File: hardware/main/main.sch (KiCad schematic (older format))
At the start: 2 parts, among them J101 Conn_01x06_Male, J102 Conn_01x06_Male

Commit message: Alimentação de 12V criada no Charger, que recebe 18V do Controller
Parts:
- removed J102: Conn_01x06_Male, symbol Connector:Conn_01x06_Male
- added J102: Conn_01x07_Male, symbol Connector:Conn_01x07_Male
- J101: value Conn_01x06_Male -> Conn_01x07_Male; symbol Connector:Conn_01x06_Male -> Connector:Conn_01x07_Male
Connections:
- net CONTROLLER/Charge: now also J102.6 (Pin_6)
- net CONTROLLER/GND: now also J102.1 (Pin_1), J102.3 (Pin_3), J102.5 (Pin_5)
- net CONTROLLER/RL_OFF: now also J102.2 (Pin_2)
- net CONTROLLER/RL_ON: now also J102.4 (Pin_4)
- new net CHARGER/+18V_IN: J101.7 (Pin_7)
- new net CONTROLLER/+18V_OUT: J102.7 (Pin_7)
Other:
- note added: "TO-DO LIST:\n [x] Separar a abstração das duas placas\n\n [x] Criar conexão entre as duas placas\n\n [x] Nomear componentes;\n\n [x] Passar alimentação para o Charger;\n\n [x] Criar fonte 12V no Charger\n\n [_] Adicionar snubbers para os relés (olhar na simulação);\n\n [_] Passar o condicionamento do sinal para o Charger;\n"
- note removed: "TO-DO LIST:\n [x] Separar a abstração das duas placas\n\n [x] Criar conexão entre as duas placas\n\n [x] Nomear componentes;\n\n [_] Passar alimentação para o Charger;\n\n [_] Adicionar snubbers para os relés (olhar na simulação);\n\n [_] Passar o condicionamento do sinal para o Charger;\n"
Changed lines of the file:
@@
 $EndDescr
 $Sheet
-S 3050 2400 1200 950
+S 3050 2400 1200 1050
 U 5C9C4D6B
 F0 "CHARGER" 50
 F1 "Charger.sch" 50
-F2 "Charge" O R 4250 2700 50
-F3 "RL_ON" O R 4250 2800 50
-F4 "RL_OFF" O R 4250 2900 50
-F5 "GND" O R 4250 3000 50
+F2 "Charge" O R 4250 2950 50
+F3 "RL_ON" O R 4250 3050 50
+F4 "RL_OFF" O R 4250 3150 50
+F5 "GND" O R 4250 2600 50
+F6 "+18V_IN" I R 4250 2500 50
 $EndSheet
 $Sheet
-S 6300 2300 1500 1250
+S 6000 2400 1250 1050
 U 5CA4DC1F
 F0 "CONTROLLER" 50
 F1 "controller.sch" 50
-F2 "RL_OFF" I L 6300 2900 50
-F3 "RL_ON" I L 6300 2800 50
-F4 "Charge" I L 6300 2700 50
-F5 "GND" I L 6300 3000 50
+F2 "RL_OFF" I L 6000 3150 50
+F3 "RL_ON" I L 6000 3050 50
+F4 "Charge" I L 6000 2950 50
+F5 "GND" I L 6000 2600 50
+F6 "+18V_OUT" I L 6000 2500 50
 $EndSheet
 $Comp
-L Connector:Conn_01x06_Male J101
+L Connector:Conn_01x07_Male J101
 U 1 1 5CA76C06
-P 4650 2900
-F 0 "J101" H 4950 3300 50  0000 R CNN
-F 1 "Conn_01x06_Male" H 4950 3200 50  0000 R CNN
-F 2 "" H 4650 2900 50  0001 C CNN
-F 3 "~" H 4650 2900 50  0001 C CNN
-	1    4650 2900
+P 4700 3050
+F 0 "J101" H 5000 3500 50  0000 R CNN
+F 1 "Conn_01x07_Male" H 5000 3400 50  0000 R CNN
+F 2 "" H 4700 3050 50  0001 C CNN
+F 3 "~" H 4700 3050 50  0001 C CNN
+	1    4700 3050
 	-1   0    0    1
 $EndComp
 Wire Wire Line
-	4250 2700 4350 2700
+	4250 3150 4350 3150
 Wire Wire Line
-	4250 2900 4350 2900
+	4350 2950 4350 2850
 Wire Wire Line
-	4350 2700 4350 2600
+	4350 2850 4500 2850
 Wire Wire Line
-	4350 2600 4450 2600
+	4250 3050 4500 3050
 Wire Wire Line
-	4250 2800 4450 2800
+	4350 3150 4350 3250
 Wire Wire Line
-	4350 2900 4350 3000
+	4350 3250 4500 3250
 Wire Wire Line
-	4350 3000 4450 3000
+	4500 2950 4400 2950
 Wire Wire Line
-	4450 2700 4400 2700
+	4400 2950 4400 3150
 Wire Wire Line
-	4400 2700 4400 2900
+	4400 3150 4500 3150
 Wire Wire Line
-	4400 2900 4450 2900
+	4400 3150 4400 3350
 Wire Wire Line
-	4400 2900 4400 3100
+	4400 3350 4500 3350
+Connection ~ 4400 3150
+Text Notes 4400 5000 0    50   ~ 0
+TO-DO LIST:\n  [x] Separar a abstração das duas placas\n\n  [x] Criar conexão entre as duas placas\n\n  [x] Nomear componentes;\n\n  [x] Passar alimentação para o Charger;\n\n  [x] Criar fonte 12V no  Charger\n\n  [_] Adicionar snubbers para os relés (olhar na simulação);\n\n  [_] Passar o condicionamento do sinal para o Charger;\n
 Wire Wire Line
-	4400 3100 4450 3100
-Connection ~ 4400 2900
+	4350 2950 4250 2950
 Wire Wire Line
-	4400 3100 4300 3100
+	4250 2600 4400 2600
 Wire Wire Line
-	4300 3100 4300 3000
+	4400 2600 4400 2950
+Connection ~ 4400 2950
 Wire Wire Line
-	4300 3000 4250 3000
-Connection ~ 4400 3100
+	4250 2500 4450 2500
+Wire Wire Line
+	4450 2500 4450 2750
+Wire Wire Line
+	4450 2750 4500 2750
 $Comp
-L Connector:Conn_01x06_Male J102
-U 1 1 5CA80272
-P 5900 2900
-F 0 "J102" H 6200 3300 50  0000 R CNN
-F 1 "Conn_01x06_Male" H 6200 3200 50  0000 R CNN
-F 2 "" H 5900 2900 50  0001 C CNN
-F 3 "~" H 5900 2900 50  0001 C CNN
-	1    5900 2900
+L Connector:Conn_01x07_Male J102
+U 1 1 5CAB450A
+P 5550 3050
+F 0 "J102" H 5850 3500 50  0000 R CNN
+F 1 "Conn_01x07_Male" H 5850 3400 50  0000 R CNN
+F 2 "" H 5550 3050 50  0001 C CNN
+F 3 "~" H 5550 3050 50  0001 C CNN
+	1    5550 3050
 	1    0    0    1
 $EndComp
 Wire Wire Line
-	6300 2700 6200 2700
+	6000 3150 5900 3150
 Wire Wire Line
-	6300 2900 6200 2900
+	5900 2950 5900 2850
 Wire Wire Line
-	6200 2700 6200 2600
+	5900 2850 5750 2850
 Wire Wire Line
-	6200 2600 6100 2600
+	6000 3050 5750 3050
 Wire Wire Line
-	6300 2800 6100 2800
+	5900 3150 5900 3250
 Wire Wire Line
-	6200 2900 6200 3000
+	5900 3250 5750 3250
 Wire Wire Line
-	6200 3000 6100 3000
+	5750 2950 5850 2950
 Wire Wire Line
-	6100 2700 6150 2700
+	5850 2950 5850 3150
 Wire Wire Line
-	6150 2700 6150 2900
+	5850 3150 5750 3150
 Wire Wire Line
-	6150 2900 6100 2900
+	5850 3150 5850 3350
 Wire Wire Line
-	6150 2900 6150 3100
+	5850 3350 5750 3350
+Connection ~ 5850 3150
 Wire Wire Line
-	6150 3100 6100 3100
-Connection ~ 6150 2900
+	5900 2950 6000 2950
 Wire Wire Line
-	6150 3100 6250 3100
+	6000 2600 5850 2600
 Wire Wire Line
-	6250 3100 6250 3000
+	5850 2600 5850 2950
+Connection ~ 5850 2950
 Wire Wire Line
-	6250 3000 6300 3000
-Connection ~ 6150 3100
-Text Notes 4400 4750 0    50   ~ 0
-TO-DO LIST:\n  [x] Separar a abstração das duas placas\n\n  [x] Criar conexão entre as duas placas\n\n  [x] Nomear componentes;\n\n  [_] Passar alimentação para o Charger;\n\n  [_] Adicionar snubbers para os relés (olhar na simulação);\n\n  [_] Passar o condicionamento do sinal para o Charger;\n
+	6000 2500 5800 2500
+Wire Wire Line
+	5800 2500 5800 2750
+Wire Wire Line
+	5800 2750 5750 2750
 $EndSCHEMATC

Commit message: Analog passado para o Charger
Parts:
- removed J102: Conn_01x07_Male, symbol Connector:Conn_01x07_Male
- added J102: Conn_01x11_Male, symbol Connector:Conn_01x11_Male
- J101: value Conn_01x07_Male -> Conn_01x11_Male; symbol Connector:Conn_01x07_Male -> Connector:Conn_01x11_Male
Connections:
- net CHARGER/+18V_IN: now also J101.11 (Pin_11); no longer J101.7 (Pin_7)
- net CHARGER/Charge: now also J101.10 (Pin_10); no longer J101.6 (Pin_6)
- net CHARGER/GND: now also J101.7 (Pin_7), J101.9 (Pin_9)
- net CHARGER/RL_OFF: now also J101.6 (Pin_6); no longer J101.2 (Pin_2)
- net CHARGER/RL_ON: now also J101.8 (Pin_8); no longer J101.4 (Pin_4)
- net CONTROLLER/+18V_OUT: now also J102.11 (Pin_11)
- net CONTROLLER/Charge: now also J102.10 (Pin_10)
- net CONTROLLER/GND: now also J102.1 (Pin_1), J102.3 (Pin_3), J102.5 (Pin_5), J102.7 (Pin_7), J102.9 (Pin_9)
- net CONTROLLER/RL_OFF: now also J102.6 (Pin_6)
- net CONTROLLER/RL_ON: now also J102.8 (Pin_8)
- new net CHARGER/sig_bat+: J101.4 (Pin_4)
- new net CHARGER/sig_cap+: J101.2 (Pin_2)
- new net CONTROLLER/sig_bat+: J102.4 (Pin_4)
- new net CONTROLLER/sig_cap+: J102.2 (Pin_2)
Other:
- note added: "TO-DO LIST:\n [x] Separar a abstração das duas placas\n\n [x] Criar conexão entre as duas placas\n\n [x] Nomear componentes;\n\n [x] Passar alimentação para o Charger;\n\n [x] Criar fonte 12V no Charger\n\n [_] Adicionar snubbers para os relés (olhar na simulação);\n\n [x] Passar o condicionamento do sinal para o Charger;\n\n [_] \n\n [_]"
- note removed: "TO-DO LIST:\n [x] Separar a abstração das duas placas\n\n [x] Criar conexão entre as duas placas\n\n [x] Nomear componentes;\n\n [x] Passar alimentação para o Charger;\n\n [x] Criar fonte 12V no Charger\n\n [_] Adicionar snubbers para os relés (olhar na simulação);\n\n [_] Passar o condicionamento do sinal para o Charger;\n"
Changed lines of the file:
@@
 $EndDescr
 $Sheet
-S 3050 2400 1200 1050
+S 3050 2400 1200 1450
 U 5C9C4D6B
 F0 "CHARGER" 50
@@
 F5 "GND" O R 4250 2600 50
 F6 "+18V_IN" I R 4250 2500 50
+F7 "sig_bat+" O R 4250 3400 50
+F8 "sig_cap+" O R 4250 3500 50
 $EndSheet
 $Sheet
-S 6000 2400 1250 1050
+S 6000 2400 1250 1450
 U 5CA4DC1F
 F0 "CONTROLLER" 50
@@
 F5 "GND" I L 6000 2600 50
 F6 "+18V_OUT" I L 6000 2500 50
+F7 "sig_bat+" I L 6000 3400 50
+F8 "sig_cap+" I L 6000 3500 50
 $EndSheet
 $Comp
-L Connector:Conn_01x07_Male J101
+L Connector:Conn_01x11_Male J101
 U 1 1 5CA76C06
-P 4700 3050
-F 0 "J101" H 5000 3500 50  0000 R CNN
-F 1 "Conn_01x07_Male" H 5000 3400 50  0000 R CNN
-F 2 "" H 4700 3050 50  0001 C CNN
-F 3 "~" H 4700 3050 50  0001 C CNN
-	1    4700 3050
+P 4700 3250
+F 0 "J101" H 5000 3950 50  0000 R CNN
+F 1 "Conn_01x11_Male" H 5000 3850 50  0000 R CNN
+F 2 "" H 4700 3250 50  0001 C CNN
+F 3 "~" H 4700 3250 50  0001 C CNN
+	1    4700 3250
 	-1   0    0    1
 $EndComp
@@
 Wire Wire Line
 	4400 3150 4400 3350
-Wire Wire Line
-	4400 3350 4500 3350
 Connection ~ 4400 3150
-Text Notes 4400 5000 0    50   ~ 0
-TO-DO LIST:\n  [x] Separar a abstração das duas placas\n\n  [x] Criar conexão entre as duas placas\n\n  [x] Nomear componentes;\n\n  [x] Passar alimentação para o Charger;\n\n  [x] Criar fonte 12V no  Charger\n\n  [_] Adicionar snubbers para os relés (olhar na simulação);\n\n  [_] Passar o condicionamento do sinal para o Charger;\n
+Text Notes 4450 5600 0    50   ~ 0
+TO-DO LIST:\n  [x] Separar a abstração das duas placas\n\n  [x] Criar conexão entre as duas placas\n\n  [x] Nomear componentes;\n\n  [x] Passar alimentação para o Charger;\n\n  [x] Criar fonte 12V no  Charger\n\n  [_] Adicionar snubbers para os relés (olhar na simulação);\n\n  [x] Passar o condicionamento do sinal para o Charger;\n\n  [_] \n\n  [_]
 Wire Wire Line
 	4350 2950 4250 2950
@@
 Wire Wire Line
 	4450 2750 4500 2750
+Wire Wire Line
+	4400 3350 4400 3550
+Wire Wire Line
+	4400 3550 4500 3550
+Connection ~ 4400 3350
+Wire Wire Line
+	4400 3550 4400 3750
+Wire Wire Line
+	4400 3750 4500 3750
+Wire Wire Line
+	4400 3350 4500 3350
+Connection ~ 4400 3550
+Wire Wire Line
+	4500 3450 4350 3450
+Wire Wire Line
+	4350 3450 4350 3400
+Wire Wire Line
+	4350 3400 4250 3400
+Wire Wire Line
+	4250 3500 4300 3500
+Wire Wire Line
+	4300 3500 4300 3650
+Wire Wire Line
+	4300 3650 4500 3650
 $Comp
-L Connector:Conn_01x07_Male J102
-U 1 1 5CAB450A
-P 5550 3050
-F 0 "J102" H 5850 3500 50  0000 R CNN
-F 1 "Conn_01x07_Male" H 5850 3400 50  0000 R CNN
-F 2 "" H 5550 3050 50  0001 C CNN
-F 3 "~" H 5550 3050 50  0001 C CNN
-	1    5550 3050
+L Connector:Conn_01x11_Male J102
+U 1 1 5CBD36A2
+P 5550 3250
+F 0 "J102" H 5850 3950 50  0000 R CNN
+F 1 "Conn_01x11_Male" H 5850 3850 50  0000 R CNN
+F 2 "" H 5550 3250 50  0001 C CNN
+F 3 "~" H 5550 3250 50  0001 C CNN
+	1    5550 3250
 	1    0    0    1
 $EndComp
@@
 Wire Wire Line
 	5850 3150 5850 3350
-Wire Wire Line
-	5850 3350 5750 3350
 Connection ~ 5850 3150
 Wire Wire Line
@@
 Wire Wire Line
 	5800 2750 5750 2750
+Wire Wire Line
+	5850 3350 5850 3550
+Wire Wire Line
+	5850 3550 5750 3550
+Connection ~ 5850 3350
+Wire Wire Line
+	5850 3550 5850 3750
+Wire Wire Line
+	5850 3750 5750 3750
+Wire Wire Line
+	5850 3350 5750 3350
+Connection ~ 5850 3550
+Wire Wire Line
+	5750 3450 5900 3450
+Wire Wire Line
+	5900 3450 5900 3400
+Wire Wire Line
+	5900 3400 6000 3400
+Wire Wire Line
+	6000 3500 5950 3500
+Wire Wire Line
+	5950 3500 5950 3650
+Wire Wire Line
+	5950 3650 5750 3650
 $EndSCHEMATC

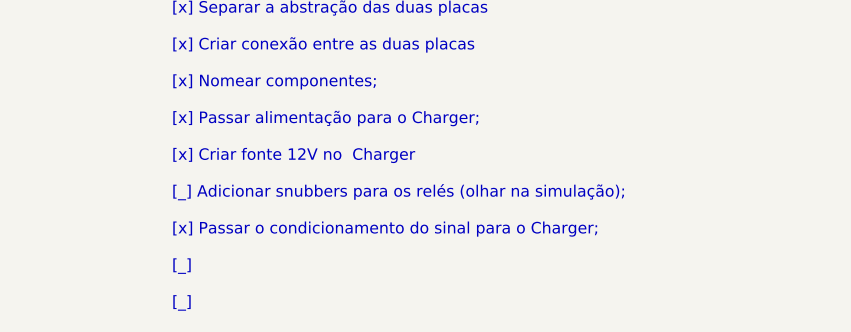
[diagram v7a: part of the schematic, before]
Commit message: Analog passado para o Charger
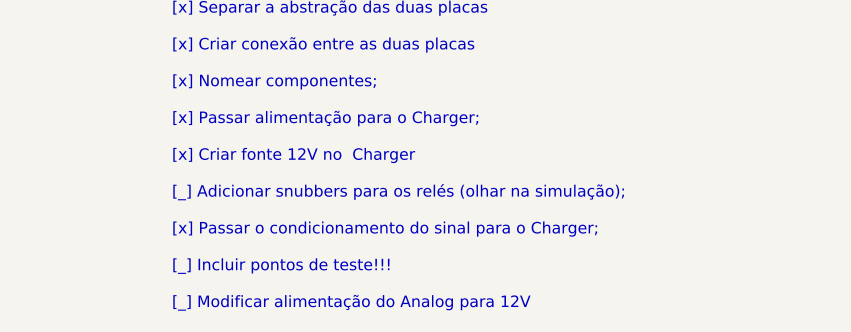
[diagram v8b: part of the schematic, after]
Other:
- note added: "TO-DO LIST:\n [x] Separar a abstração das duas placas\n\n [x] Criar conexão entre as duas placas\n\n [x] Nomear componentes;\n\n [x] Passar alimentação para o Charger;\n\n [x] Criar fonte 12V no Charger\n\n [_] Adicionar snubbers para os relés (olhar na simulação);\n\n [x] Passar o condicionamento do sinal para o Charger;\n\n [_] Incluir pontos de teste!!!\n\n [_] Modificar alimentação do Analog 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"
- note removed: "TO-DO LIST:\n [x] Separar a abstração das duas placas\n\n [x] Criar conexão entre as duas placas\n\n [x] Nomear componentes;\n\n [x] Passar alimentação para o Charger;\n\n [x] Criar fonte 12V no Charger\n\n [_] Adicionar snubbers para os relés (olhar na simulação);\n\n [x] Passar o condicionamento do sinal para o Charger;\n\n [_] \n\n [_]"
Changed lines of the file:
@@
 Connection ~ 4400 3150
 Text Notes 4450 5600 0    50   ~ 0
-TO-DO LIST:\n  [x] Separar a abstração das duas placas\n\n  [x] Criar conexão entre as duas placas\n\n  [x] Nomear componentes;\n\n  [x] Passar alimentação para o Charger;\n\n  [x] Criar fonte 12V no  Charger\n\n  [_] Adicionar snubbers para os relés (olhar na simulação);\n\n  [x] Passar o condicionamento do sinal para o Charger;\n\n  [_] \n\n  [_]
+TO-DO LIST:\n  [x] Separar a abstração das duas placas\n\n  [x] Criar conexão entre as duas placas\n\n  [x] Nomear componentes;\n\n  [x] Passar alimentação para o Charger;\n\n  [x] Criar fonte 12V no  Charger\n\n  [_] Adicionar snubbers para os relés (olhar na simulação);\n\n  [x] Passar o condicionamento do sinal para o Charger;\n\n  [_] Incluir pontos de teste!!!\n\n  [_] Modificar alimentação do Analog para 12V
 Wire Wire Line
 	4350 2950 4250 2950
